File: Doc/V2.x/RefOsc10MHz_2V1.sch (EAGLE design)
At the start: 82 parts, among them CON1 TYCO-AMP_USBUSB-B_SMT, CON2 HEADER-2X5SMD, CON3 SD-73100-0105, CON4 AVR-ISP-6SMD, CON5 AVR-JTAG-10SMD, CON6 HEADER-2X3SMD, CON7 MCX-J-P-X-RA-SM1, IC1 ATmega328-P, IC2 LC4032V_XXT44, IC3 74HCT221D, IC6 LM2831YMF, IC7 CFPT-141, IC8 712-RXM-GNSS-TM-B, U5 OPA354

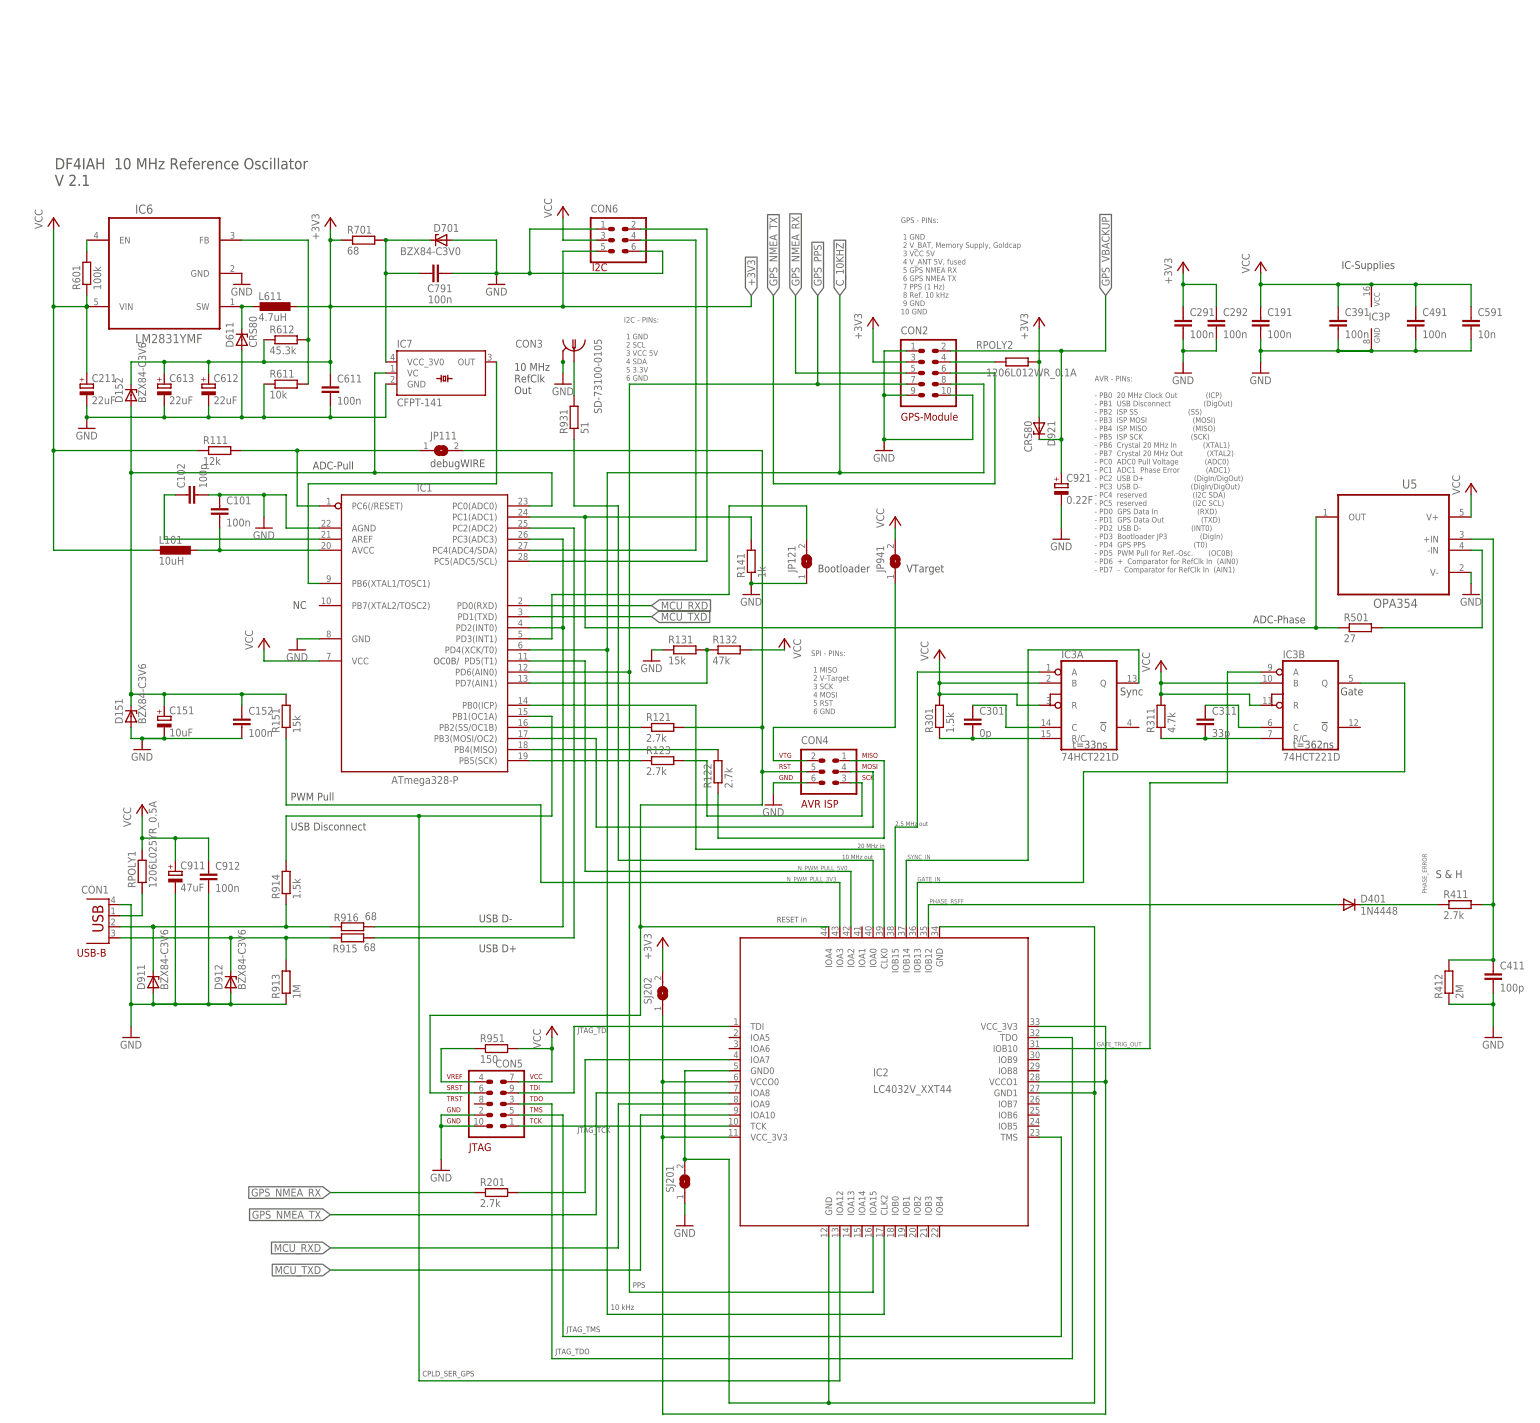
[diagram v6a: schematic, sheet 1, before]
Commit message: avr_DF4IAH_Bootloader - Doc - Eagle: V2.1 - LcdModule-16x2_1V0 added, updates for RefOsc10MHz_2V1 also
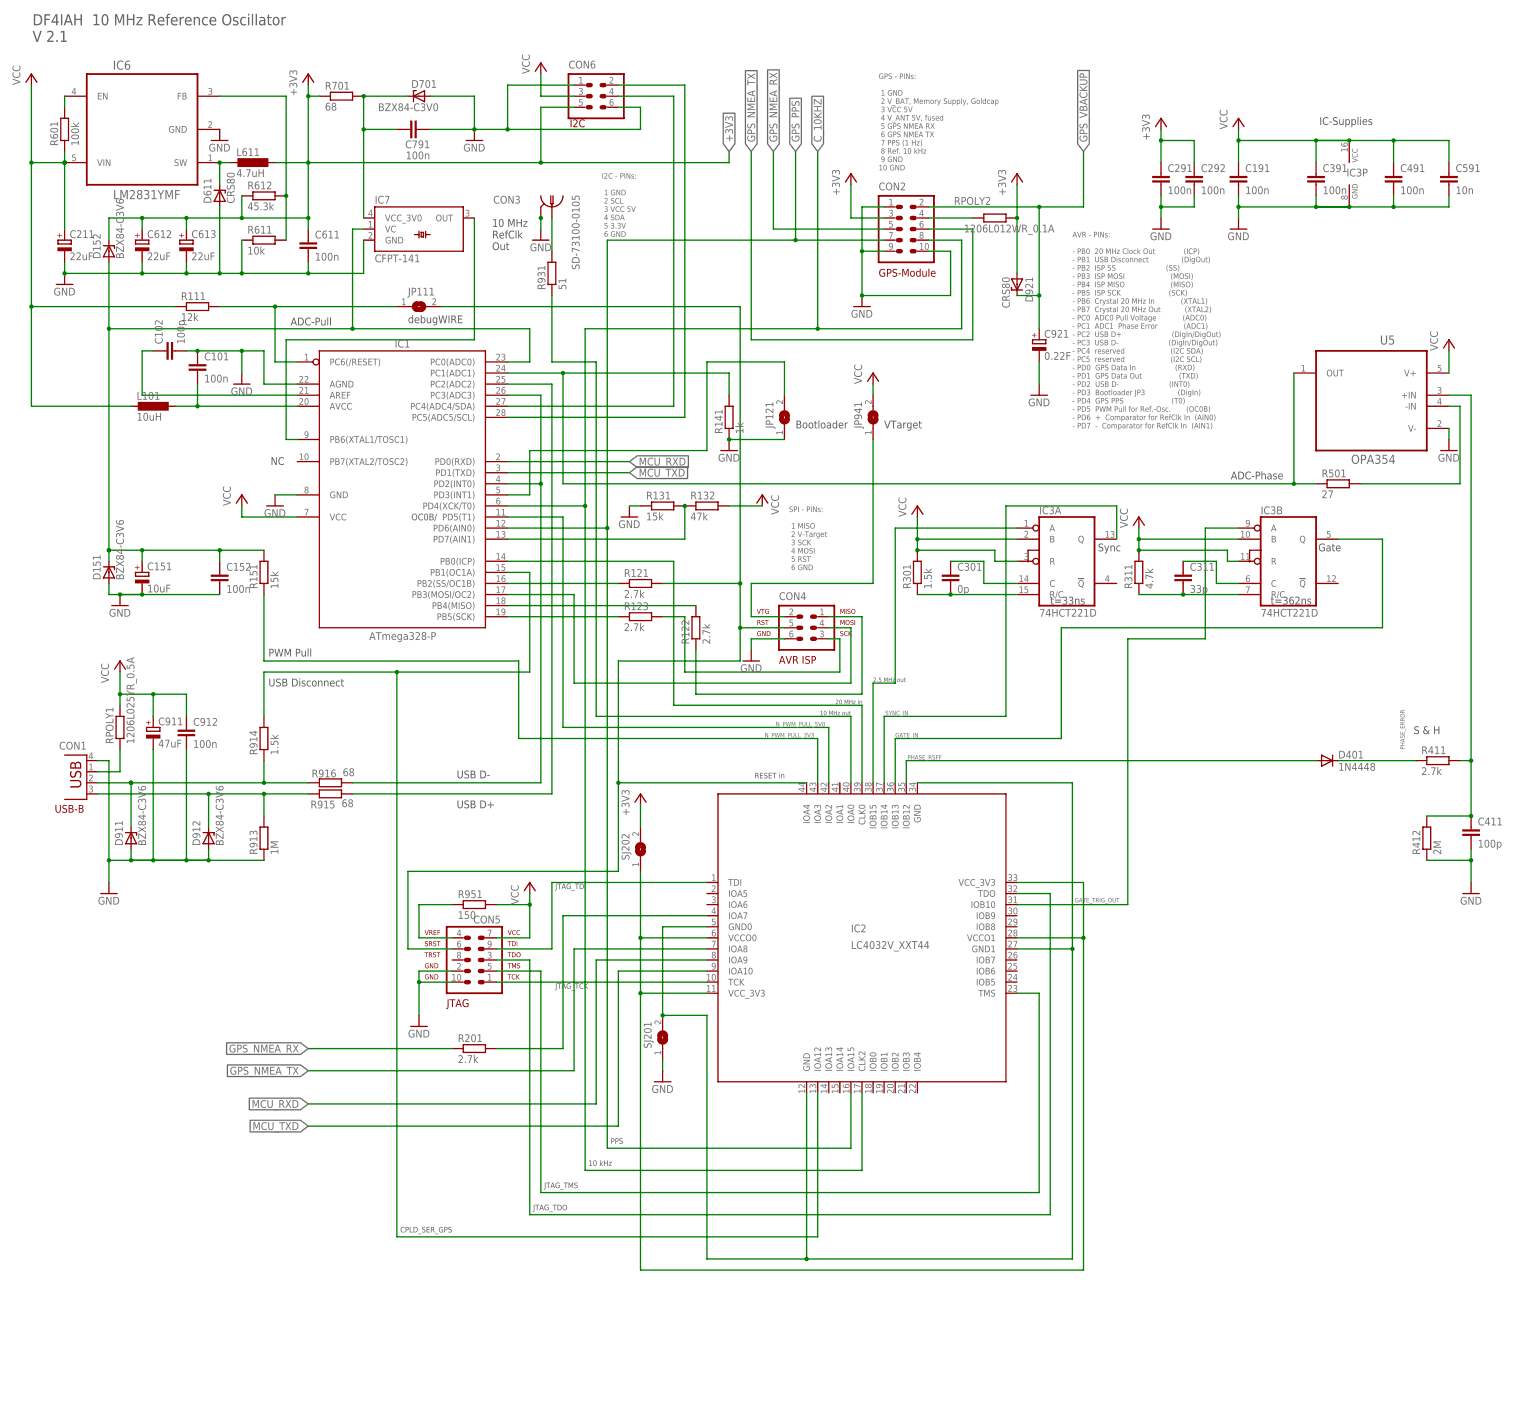
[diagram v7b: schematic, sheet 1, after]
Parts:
- C211, C612, C613: device rcl:CPOL-EUA/3216-18W -> rcl:CPOL-EUB
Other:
- moved on the sheet: C101, C102, C151, C152, C191, C211, C291, C292, C301, C311, C391, C411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

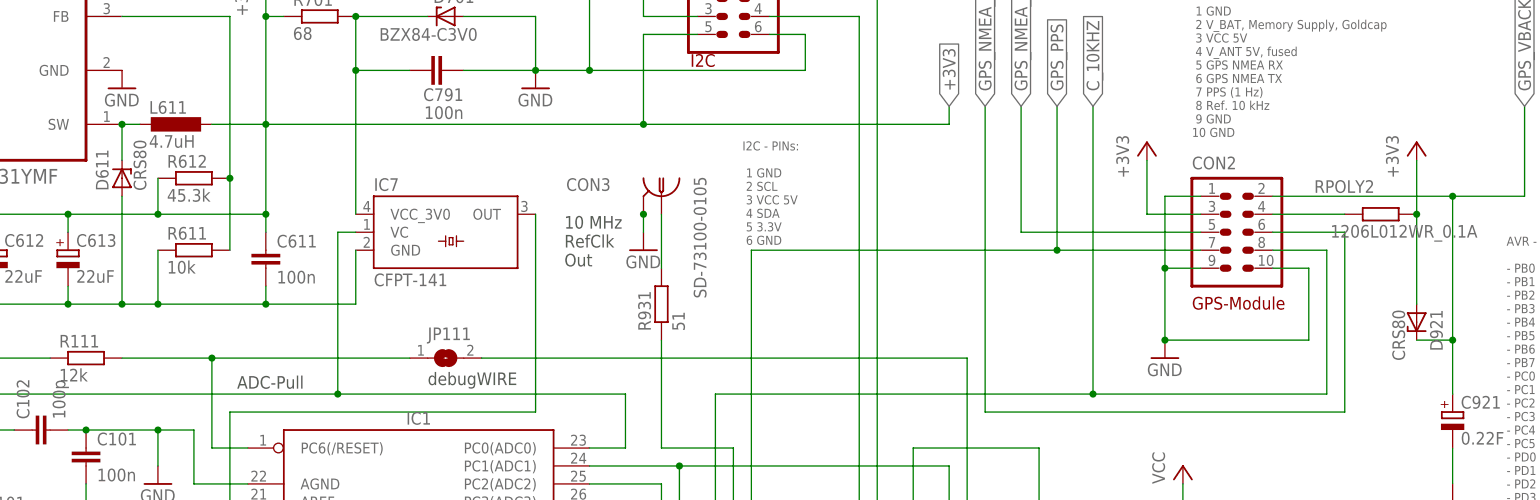
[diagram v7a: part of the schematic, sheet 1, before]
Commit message: avr_DF4IAH_Bootloader - Doc - Eagle: V2.1 - correction: CRS80 --> CRS08
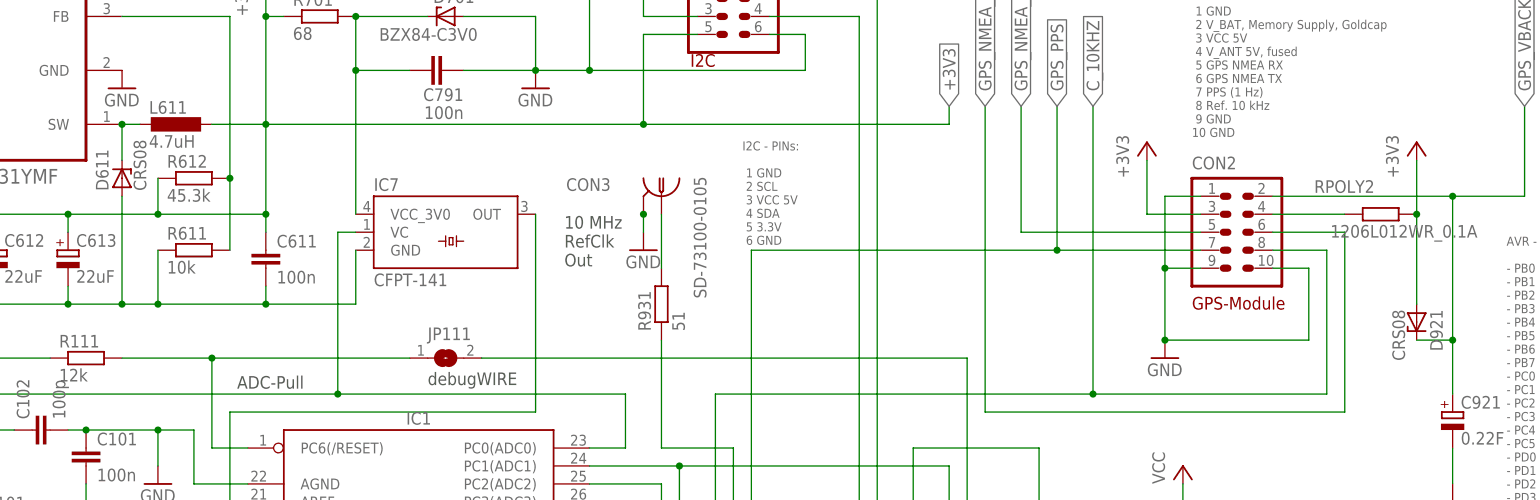
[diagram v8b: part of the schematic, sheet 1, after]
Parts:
- D611, D921: value CRS80 -> CRS08
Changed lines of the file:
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@@
 <part name="GND24" library="supply1" deviceset="GND" device=""/>
 <part name="C921" library="rcl" deviceset="CPOL-EU" device="140CLH-1010" value="0.22F"/>
-<part name="D611" library="diode" deviceset="ZENER-DIODE" device="SOD80C" value="CRS80"/>
-<part name="D921" library="diode" deviceset="ZENER-DIODE" device="SOD80C" value="CRS80"/>
+<part name="D611" library="diode" deviceset="ZENER-DIODE" device="SOD80C" value="CRS08"/>
+<part name="D921" library="diode" deviceset="ZENER-DIODE" device="SOD80C" value="CRS08"/>
 <part name="D701" library="diode" deviceset="BZX84CSMD" device="" value="BZX84-C3V0"/>
 <part name="R701" library="rcl" deviceset="R-EU_" device="R0805" value="68"/>
